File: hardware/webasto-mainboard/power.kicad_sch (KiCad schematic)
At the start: 14 parts, among them U5 BD9G341EFJ

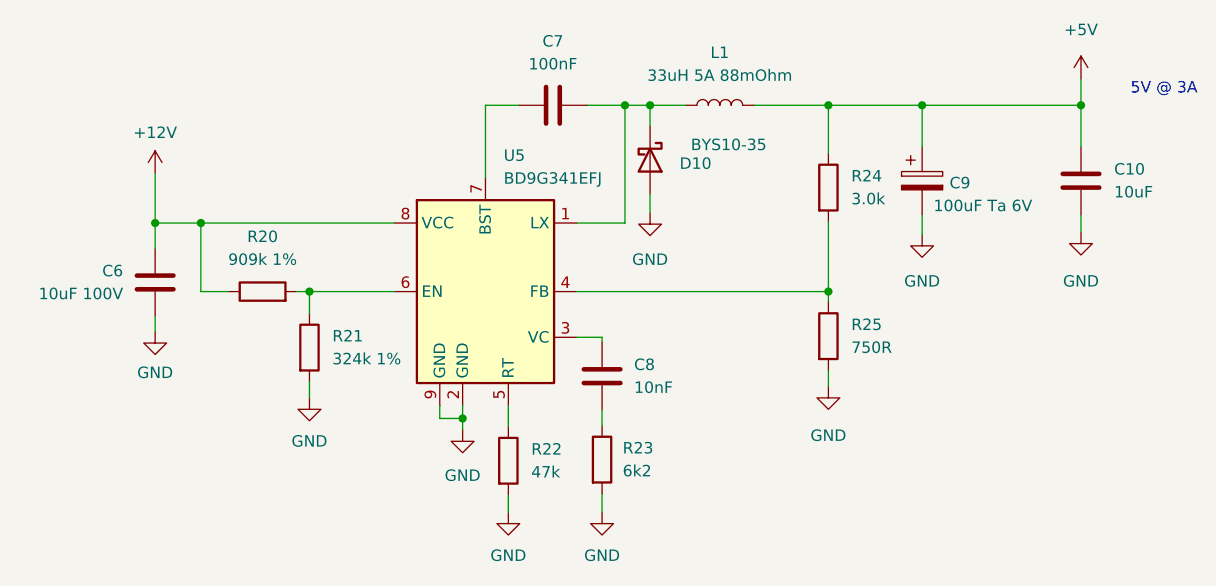
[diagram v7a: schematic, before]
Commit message: Move the LED to the mainboard
- due to how the driver doesn't share the SPI bus well, you currently can
  either use the TCP stack or the GPIOs.  Mixing will cause weird crashes.
- so I'm adding the LED onto the mainboard directly.
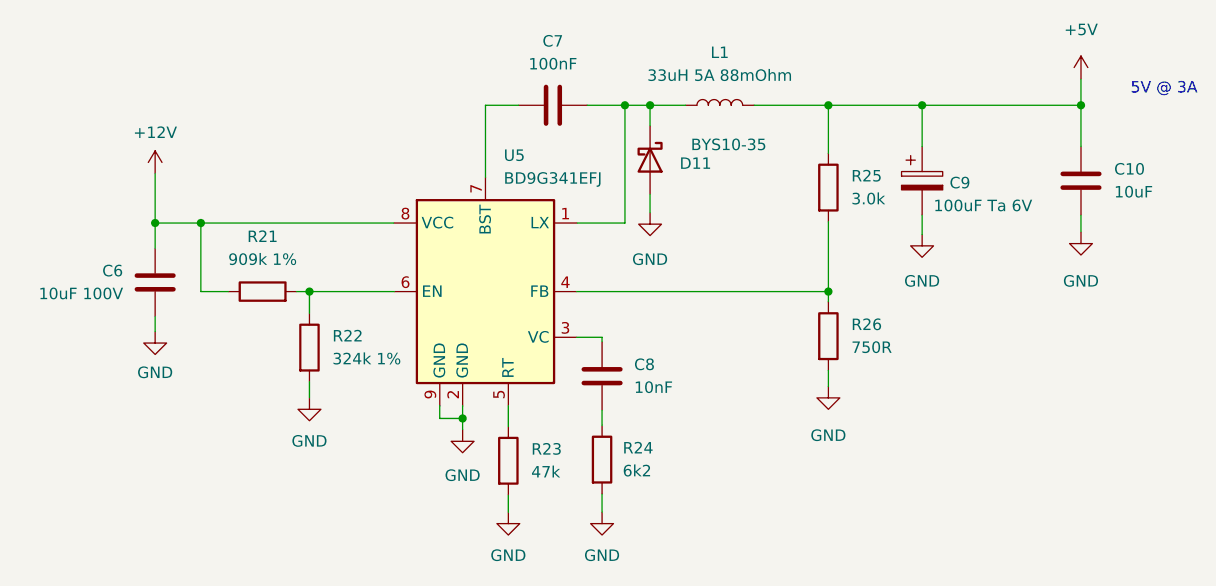
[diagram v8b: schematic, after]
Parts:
- renumbered D10 to D11, R20 to R21, R21 to R22, R22 to R23, R23 to R24, R24 to R25, R25 to R26
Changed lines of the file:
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@@
   (symbol (lib_id "Device:D_Schottky") (at 163.068 65.278 270) (unit 1)
     (in_bom yes) (on_board yes)
-    (property "Reference" "D10" (id 0) (at 169.9006 65.659 90)
+    (property "Reference" "D11" (id 0) (at 169.9006 65.659 90)
       (effects (font (size 1.27 1.27)) (justify right))
     )
@@
   (symbol (lib_id "Device:R") (at 125.222 86.106 0) (unit 1)
     (in_bom yes) (on_board yes) (fields_autoplaced)
-    (property "Reference" "R21" (id 0) (at 127.762 84.8359 0)
+    (property "Reference" "R22" (id 0) (at 127.762 84.8359 0)
       (effects (font (size 1.27 1.27)) (justify left))
     )
@@
   (symbol (lib_id "power:GND") (at 210.947 73.279 0) (unit 1)
     (in_bom yes) (on_board yes) (fields_autoplaced)
-    (property "Reference" "#PWR060" (id 0) (at 210.947 79.629 0)
+    (property "Reference" "#PWR061" (id 0) (at 210.947 79.629 0)
       (effects (font (size 1.27 1.27)) hide)
     )
@@
   (symbol (lib_id "Device:R") (at 147.32 98.679 0) (unit 1)
     (in_bom yes) (on_board yes) (fields_autoplaced)
-    (property "Reference" "R22" (id 0) (at 149.86 97.4089 0)
+    (property "Reference" "R23" (id 0) (at 149.86 97.4089 0)
       (effects (font (size 1.27 1.27)) (justify left))
     )
@@
   (symbol (lib_id "power:GND") (at 163.068 71.12 0) (unit 1)
     (in_bom yes) (on_board yes) (fields_autoplaced)
-    (property "Reference" "#PWR056" (id 0) (at 163.068 77.47 0)
+    (property "Reference" "#PWR057" (id 0) (at 163.068 77.47 0)
       (effects (font (size 1.27 1.27)) hide)
     )
@@
   (symbol (lib_id "Device:R") (at 182.88 68.326 0) (unit 1)
     (in_bom yes) (on_board yes) (fields_autoplaced)
-    (property "Reference" "R24" (id 0) (at 185.42 67.0559 0)
+    (property "Reference" "R25" (id 0) (at 185.42 67.0559 0)
       (effects (font (size 1.27 1.27)) (justify left))
     )
@@
   (symbol (lib_id "power:GND") (at 193.294 73.533 0) (unit 1)
     (in_bom yes) (on_board yes) (fields_autoplaced)
-    (property "Reference" "#PWR058" (id 0) (at 193.294 79.883 0)
+    (property "Reference" "#PWR059" (id 0) (at 193.294 79.883 0)
       (effects (font (size 1.27 1.27)) hide)
     )
@@
   (symbol (lib_id "Device:R") (at 182.88 84.836 0) (unit 1)
     (in_bom yes) (on_board yes) (fields_autoplaced)
-    (property "Reference" "R25" (id 0) (at 185.42 83.5659 0)
+    (property "Reference" "R26" (id 0) (at 185.42 83.5659 0)
       (effects (font (size 1.27 1.27)) (justify left))
     )
@@
   (symbol (lib_id "power:GND") (at 108.077 84.328 0) (unit 1)
     (in_bom yes) (on_board yes) (fields_autoplaced)
-    (property "Reference" "#PWR051" (id 0) (at 108.077 90.678 0)
+    (property "Reference" "#PWR052" (id 0) (at 108.077 90.678 0)
       (effects (font (size 1.27 1.27)) hide)
     )
@@
   (symbol (lib_id "power:GND") (at 142.24 95.25 0) (unit 1)
     (in_bom yes) (on_board yes) (fields_autoplaced)
-    (property "Reference" "#PWR053" (id 0) (at 142.24 101.6 0)
+    (property "Reference" "#PWR054" (id 0) (at 142.24 101.6 0)
       (effects (font (size 1.27 1.27)) hide)
     )
@@
   (symbol (lib_id "power:GND") (at 125.222 91.694 0) (unit 1)
     (in_bom yes) (on_board yes) (fields_autoplaced)
-    (property "Reference" "#PWR052" (id 0) (at 125.222 98.044 0)
+    (property "Reference" "#PWR053" (id 0) (at 125.222 98.044 0)
       (effects (font (size 1.27 1.27)) hide)
     )
@@
   (symbol (lib_id "power:+12V") (at 108.077 66.802 0) (unit 1)
     (in_bom yes) (on_board yes) (fields_autoplaced)
-    (property "Reference" "#PWR050" (id 0) (at 108.077 70.612 0)
+    (property "Reference" "#PWR051" (id 0) (at 108.077 70.612 0)
       (effects (font (size 1.27 1.27)) hide)
     )
@@
   (symbol (lib_id "power:GND") (at 182.88 90.424 0) (unit 1)
     (in_bom yes) (on_board yes) (fields_autoplaced)
-    (property "Reference" "#PWR057" (id 0) (at 182.88 96.774 0)
+    (property "Reference" "#PWR058" (id 0) (at 182.88 96.774 0)
       (effects (font (size 1.27 1.27)) hide)
     )
@@
   (symbol (lib_id "power:+5V") (at 210.947 56.261 0) (unit 1)
     (in_bom yes) (on_board yes) (fields_autoplaced)
-    (property "Reference" "#PWR059" (id 0) (at 210.947 60.071 0)
+    (property "Reference" "#PWR060" (id 0) (at 210.947 60.071 0)
       (effects (font (size 1.27 1.27)) hide)
     )
@@
   (symbol (lib_id "Device:R") (at 120.015 79.883 90) (unit 1)
     (in_bom yes) (on_board yes) (fields_autoplaced)
-    (property "Reference" "R20" (id 0) (at 120.015 73.787 90))
+    (property "Reference" "R21" (id 0) (at 120.015 73.787 90))
     (property "Value" "909k 1%" (id 1) (at 120.015 76.327 90))
     (property "Footprint" "Resistor_SMD:R_0805_2012Metric_Pad1.20x1.40mm_HandSolder" (id 2) (at 120.015 81.661 90)
@@
   (symbol (lib_id "power:GND") (at 147.32 104.394 0) (unit 1)
     (in_bom yes) (on_board yes) (fields_autoplaced)
-    (property "Reference" "#PWR054" (id 0) (at 147.32 110.744 0)
+    (property "Reference" "#PWR055" (id 0) (at 147.32 110.744 0)
       (effects (font (size 1.27 1.27)) hide)
     )
@@
   (symbol (lib_id "Device:R") (at 157.734 98.552 0) (unit 1)
     (in_bom yes) (on_board yes) (fields_autoplaced)
-    (property "Reference" "R23" (id 0) (at 160.02 97.2819 0)
+    (property "Reference" "R24" (id 0) (at 160.02 97.2819 0)
       (effects (font (size 1.27 1.27)) (justify left))
     )
@@
   (symbol (lib_id "power:GND") (at 157.734 104.394 0) (unit 1)
     (in_bom yes) (on_board yes) (fields_autoplaced)
-    (property "Reference" "#PWR055" (id 0) (at 157.734 110.744 0)
-      (effects (font (size 1.27 1.27)) hide)
-    )
+    (property "Reference" "#PWR056" (id 0) (at 157.734 110.744 0)
+      (effects (font (size 1.27 1.27)) hide)
+    )
